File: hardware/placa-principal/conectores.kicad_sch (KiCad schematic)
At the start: 10 parts, among them CN1 CN1 interface (borda 2x18)

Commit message: Esquema: placa da fonte e medidas do teclado, pull-ups e /OE
- Folha Fonte (fonte.kicad_sch), levantada das fotos dos dois lados da
  placa: ponte com derivação central, 7805, 7812, 7905 com bomba de carga,
  backup da RAM (+3V_BAT) e conector de saída. Explica os ~11 V no +5 V
  quando a fonte é testada sem carga.
- Teclado medido: U16 (74LS273) e U22 (74LS244) ligam D0-D7 com os mesmos
  pinos da revista (Fig. 14), e o /CLR do U16 vai ao +5 V. O conector das
  membranas é o CN3: pino 1 embaixo à esquerda, ímpares = membrana inferior
  (linhas, U16), pares = superior (colunas, U22 e R52-R59), tudo medido.
- CN2 = entrada da fonte na placa principal.
- R30 é o pull-up do /HALT e R29 o do /IRQ; /OE da EPROM e das duas
  µPD41416 no GND (medidos).
- Roteiro de continuidade: 38 redes medidas, 6 parciais, 39 só da revista.
  Docs (hardware, teclado, origem) atualizados.

Co-Authored-By: Claude Opus 5.5 <noreply@anthropic.com>
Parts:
- added CN2: Alimentação (da fonte), Connector_PinHeader_2.54mm:PinHeader_1x05_P2.54mm_Vertical, symbol Connector_Generic:Conn_01x05
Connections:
- net +3V_BAT: now also CN2.3 (Pin_3)
- net +5V: now also CN2.2 (Pin_2)
- net -5V: now also CN2.1 (Pin_1)
- net GND: now also CN2.5 (Pin_5)
- new net +12V: CN2.4 (Pin_4)
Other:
- note added: "Alimentação: vem da placa da fonte (CN201, folha Fonte) pelo CN2, de 5 vias: -5V, +5V, +3V_BAT, +12V e GND, na ordem da etiqueta (não medida no CN2). +3V_BAT alimenta a RAM (pino 28): cerca de 5 V com o aparelho ligado, 3 V da bateria desligado (OU com os diodos D207 e D208 da fonte). +12 V e -5 V servem sobretudo à parte analógica."
- note removed: "Alimentação: vem da placa da fonte (7805 e reguladores) por um conector de pinagem não levantada: +5V, +12V, -5V, +3V_BAT e GND. +3V_BAT alimenta a RAM (pino 28): +5 V com o aparelho ligado, 3 V da bateria desligado (OU com diodos na fonte, como na revista). +12 V e -5 V servem sobretudo à parte analógica."

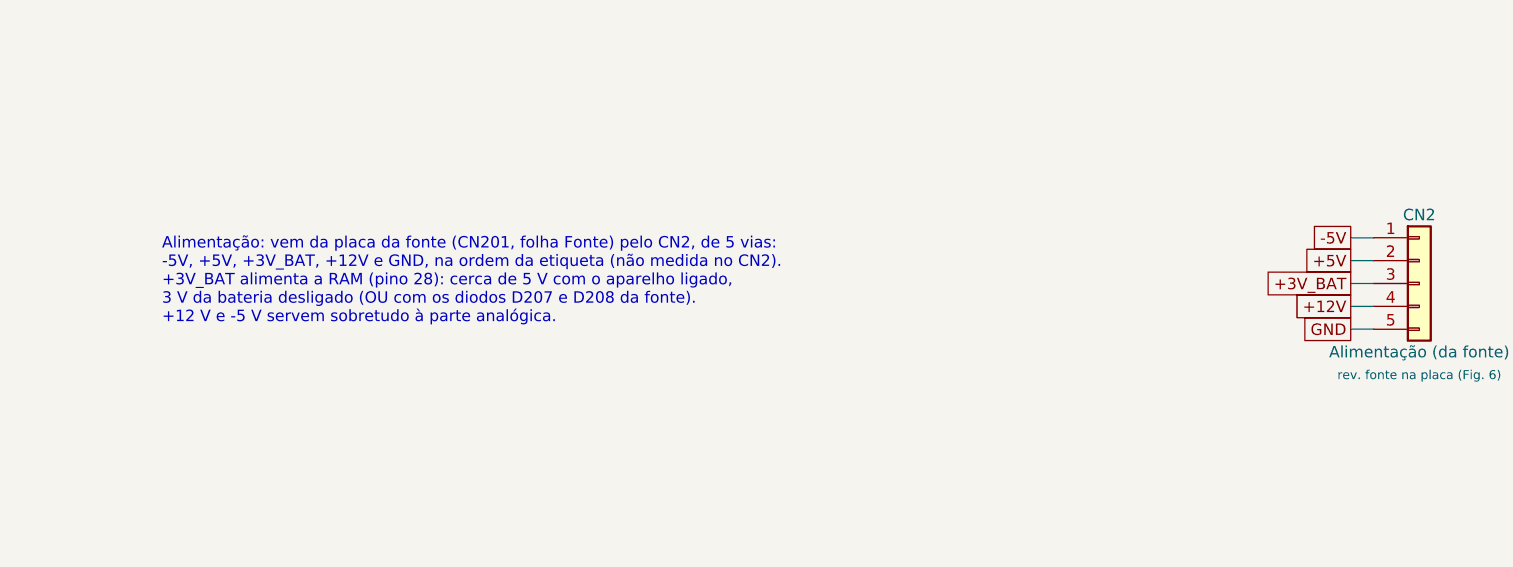
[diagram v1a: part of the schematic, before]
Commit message: Placa principal: CN2 e seleção do teclado medidos, fonte consertada
- CN2 medido: ordem inversa da do CN201 da fonte (GND no pino 1, -5 V no
  pino 5). Esquema, roteiro e docs corrigidos.
- Seleção do teclado medida: U15 pino 10 no clock do U16 e pino 9 nos
  enables do U22, como na revista. Roteiro: 40 redes medidas, 6 parciais,
  37 só da revista.
- Fonte: D210 identificado (1N4148, estava aberto); trocados D207, D208,
  D210, C203, C205 e R201. Tabela com as tensões medidas depois do
  conserto e carga de teste corrigida para 47 ohms (a de 100 ohms puxa
  menos que os ~60 mA do R201). O VET liga e mostra a abertura.

Trabalho feito em outra sessão, commitado sem alterações.

Co-Authored-By: Claude Opus 5.5 <noreply@anthropic.com>
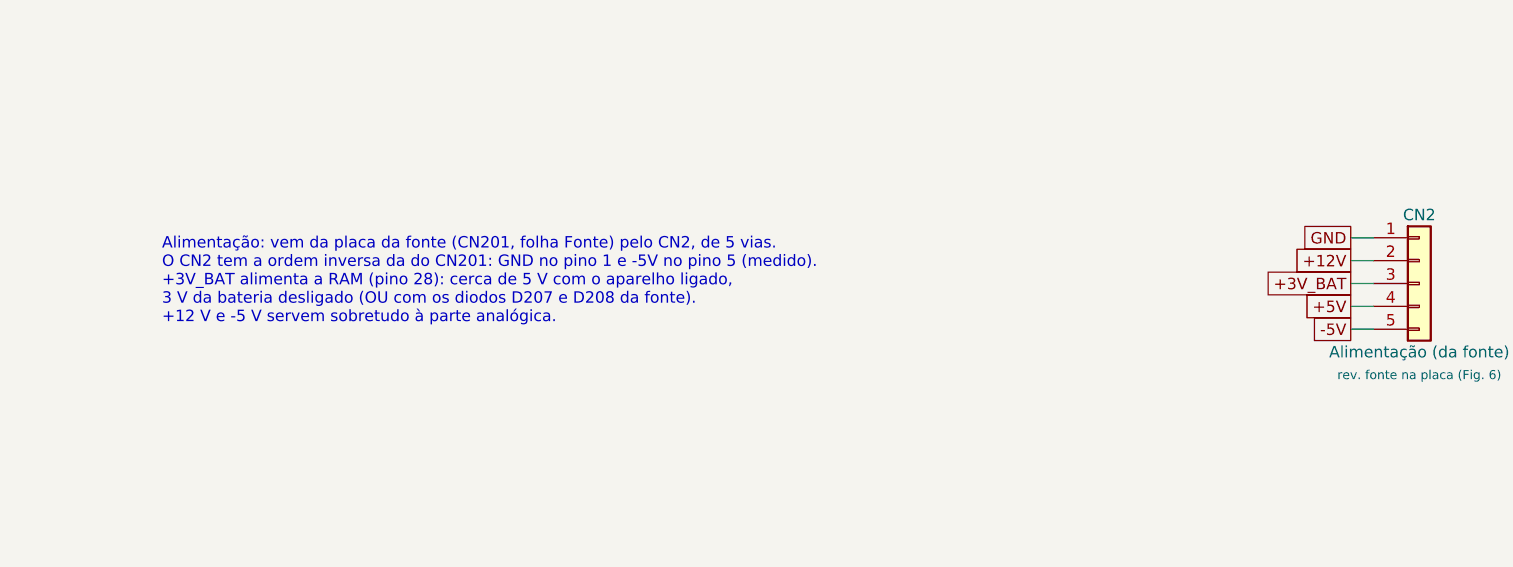
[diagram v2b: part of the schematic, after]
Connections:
- net +12V: now also CN2.2 (Pin_2); no longer CN2.4 (Pin_4)
- net +5V: now also CN2.4 (Pin_4); no longer CN2.2 (Pin_2)
- net -5V: now also CN2.5 (Pin_5); no longer CN2.1 (Pin_1)
- net GND: now also CN2.1 (Pin_1); no longer CN2.5 (Pin_5)
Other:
- note added: "Alimentação: vem da placa da fonte (CN201, folha Fonte) pelo CN2, de 5 vias. O CN2 tem a ordem inversa da do CN201: GND no pino 1 e -5V no pino 5 (medido). +3V_BAT alimenta a RAM (pino 28): cerca de 5 V com o aparelho ligado, 3 V da bateria desligado (OU com os diodos D207 e D208 da fonte). +12 V e -5 V servem sobretudo à parte analógica."
- note removed: "Alimentação: vem da placa da fonte (CN201, folha Fonte) pelo CN2, de 5 vias: -5V, +5V, +3V_BAT, +12V e GND, na ordem da etiqueta (não medida no CN2). +3V_BAT alimenta a RAM (pino 28): cerca de 5 V com o aparelho ligado, 3 V da bateria desligado (OU com os diodos D207 e D208 da fonte). +12 V e -5 V servem sobretudo à parte analógica."
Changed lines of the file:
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@@
 		)
 	)
-	(text "Alimentação: vem da placa da fonte (CN201, folha Fonte) pelo CN2, de 5 vias:\n-5V, +5V, +3V_BAT, +12V e GND, na ordem da etiqueta (não medida no CN2).\n+3V_BAT alimenta a RAM (pino 28): cerca de 5 V com o aparelho ligado,\n3 V da bateria desligado (OU com os diodos D207 e D208 da fonte).\n+12 V e -5 V servem sobretudo à parte analógica."
+	(text "Alimentação: vem da placa da fonte (CN201, folha Fonte) pelo CN2, de 5 vias.\nO CN2 tem a ordem inversa da do CN201: GND no pino 1 e -5V no pino 5 (medido).\n+3V_BAT alimenta a RAM (pino 28): cerca de 5 V com o aparelho ligado,\n3 V da bateria desligado (OU com os diodos D207 e D208 da fonte).\n+12 V e -5 V servem sobretudo à parte analógica."
 		(exclude_from_sim no)
 		(at 203.2 101.6 0)
@@
 		)
 	)
+	(global_label "GND"
+		(shape passive)
+		(at 335.28 101.6 180)
+		(fields_autoplaced yes)
+		(effects
+			(font
+				(size 1.27 1.27)
+			)
+			(justify right)
+		)
+		(property "Intersheetrefs" "${INTERSHEET_REFS}"
+			(at 335.28 101.6 0)
+			(effects
+				(font
+					(size 1.27 1.27)
+				)
+				(justify right)
+				(hide yes)
+			)
+		)
+	)
+	(global_label "+12V"
+		(shape passive)
+		(at 335.28 104.14 180)
+		(fields_autoplaced yes)
+		(effects
+			(font
+				(size 1.27 1.27)
+			)
+			(justify right)
+		)
+		(property "Intersheetrefs" "${INTERSHEET_REFS}"
+			(at 335.28 104.14 0)
+			(effects
+				(font
+					(size 1.27 1.27)
+				)
+				(justify right)
+				(hide yes)
+			)
+		)
+	)
+	(global_label "+3V_BAT"
+		(shape passive)
+		(at 335.28 106.68 180)
+		(fields_autoplaced yes)
+		(effects
+			(font
+				(size 1.27 1.27)
+			)
+			(justify right)
+		)
+		(property "Intersheetrefs" "${INTERSHEET_REFS}"
+			(at 335.28 106.68 0)
+			(effects
+				(font
+					(size 1.27 1.27)
+				)
+				(justify right)
+				(hide yes)
+			)
+		)
+	)
+	(global_label "+5V"
+		(shape passive)
+		(at 335.28 109.22 180)
+		(fields_autoplaced yes)
+		(effects
+			(font
+				(size 1.27 1.27)
+			)
+			(justify right)
+		)
+		(property "Intersheetrefs" "${INTERSHEET_REFS}"
+			(at 335.28 109.22 0)
+			(effects
+				(font
+					(size 1.27 1.27)
+				)
+				(justify right)
+				(hide yes)
+			)
+		)
+	)
 	(global_label "-5V"
 		(shape passive)
-		(at 335.28 101.6 180)
-		(fields_autoplaced yes)
-		(effects
-			(font
-				(size 1.27 1.27)
-			)
-			(justify right)
-		)
-		(property "Intersheetrefs" "${INTERSHEET_REFS}"
-			(at 335.28 101.6 0)
-			(effects
-				(font
-					(size 1.27 1.27)
-				)
-				(justify right)
-				(hide yes)
-			)
-		)
-	)
-	(global_label "+5V"
-		(shape passive)
-		(at 335.28 104.14 180)
-		(fields_autoplaced yes)
-		(effects
-			(font
-				(size 1.27 1.27)
-			)
-			(justify right)
-		)
-		(property "Intersheetrefs" "${INTERSHEET_REFS}"
-			(at 335.28 104.14 0)
-			(effects
-				(font
-					(size 1.27 1.27)
-				)
-				(justify right)
-				(hide yes)
-			)
-		)
-	)
-	(global_label "+3V_BAT"
-		(shape passive)
-		(at 335.28 106.68 180)
-		(fields_autoplaced yes)
-		(effects
-			(font
-				(size 1.27 1.27)
-			)
-			(justify right)
-		)
-		(property "Intersheetrefs" "${INTERSHEET_REFS}"
-			(at 335.28 106.68 0)
-			(effects
-				(font
-					(size 1.27 1.27)
-				)
-				(justify right)
-				(hide yes)
-			)
-		)
-	)
-	(global_label "+12V"
-		(shape passive)
-		(at 335.28 109.22 180)
-		(fields_autoplaced yes)
-		(effects
-			(font
-				(size 1.27 1.27)
-			)
-			(justify right)
-		)
-		(property "Intersheetrefs" "${INTERSHEET_REFS}"
-			(at 335.28 109.22 0)
-			(effects
-				(font
-					(size 1.27 1.27)
-				)
-				(justify right)
-				(hide yes)
-			)
-		)
-	)
-	(global_label "GND"
-		(shape passive)
 		(at 335.28 111.76 180)
